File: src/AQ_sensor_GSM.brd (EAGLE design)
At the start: 109.8 x 66.2 mm, 187 parts, among them J1 F-1X03-SIP-100-32, J2 53261-0871, J4 S8411-45R, Q2 MMBT2222, Q3 MMBT2222, Q4 MMBT2222, Q5 MMBT2222, Q6 MMBT2222, Q7 MMBT2222, Q8 FS8205, T1 S8050, T2 S8050, U1 CP2102N-A02-GQFN28, U2 DS1307Z, U3 TP4056, U4 TPS63802DLAR, U5 TXS0108EPWR, U6 TPS63802DLAR, U7 TPS63802DLAR, U8 AMS1117-3.3, X1 ESP32-S3-WROOM-1-N16R8, Y1 32.768kHz

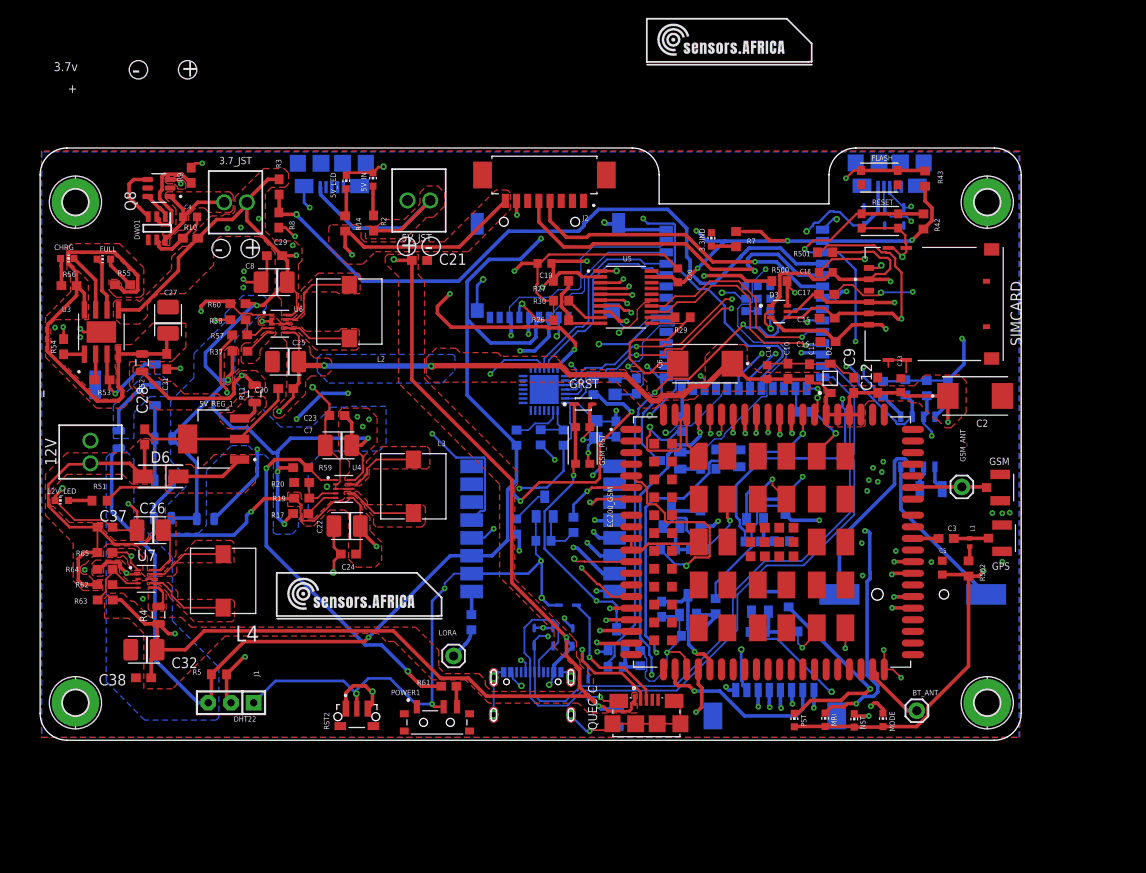
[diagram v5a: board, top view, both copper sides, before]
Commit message: Add 1.8V LDO, EC200UCN Firmware Boot Circuitry, GSM Patch Antenna
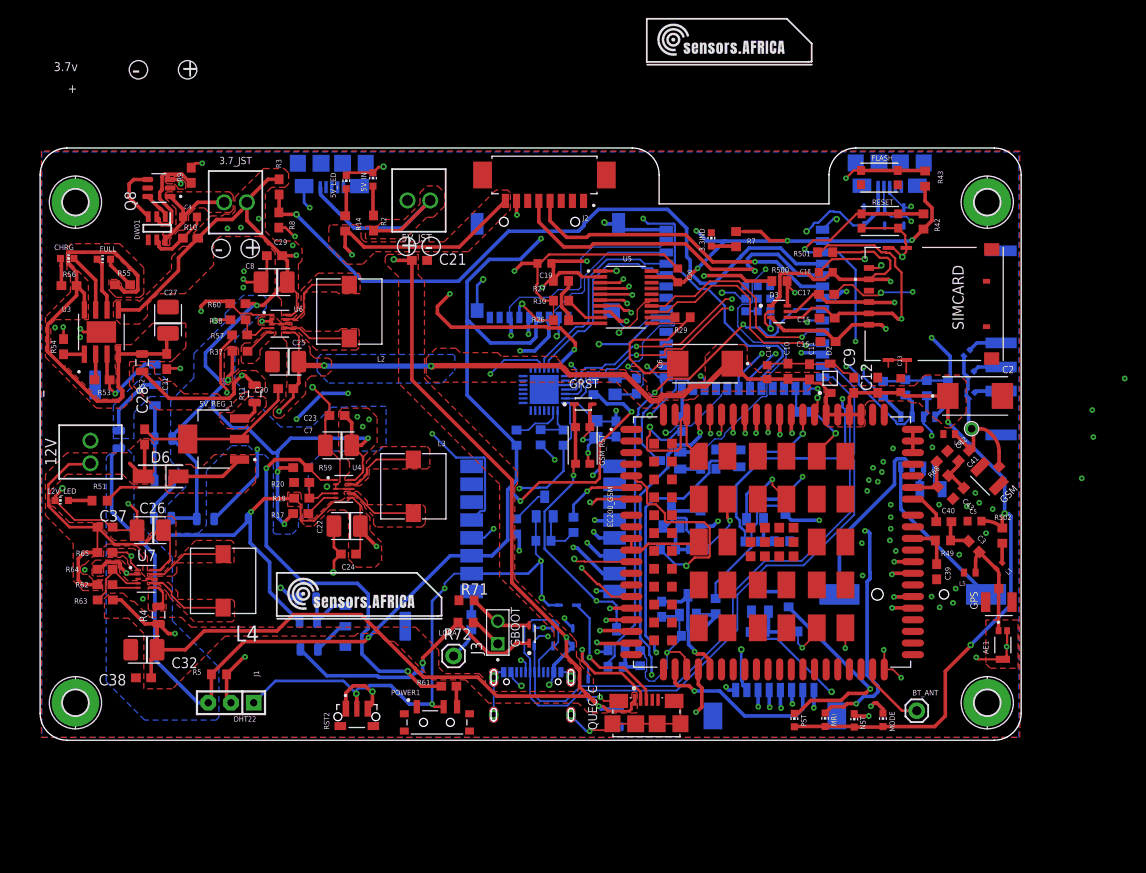
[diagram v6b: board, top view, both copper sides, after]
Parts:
- removed GSM_ANT: 1.9Ghz - 2.4Ghz, SparkFun-Connectors:1X01
- added AE1: W3011, W3011:XDCR_W3011
- added C39, C40, C41, C42, C43: 100pF, SparkFun-Capacitors:0603
- added GBOOT: ON_SEMI_1N4148WSON_SEMI_1N4148WS_0_0, AQ_sensor_GSM:ON_SEMI_1N4148WS_0
- added J3: DS1021-1X2SF162-B, DS1021-1X2SF162-B:CONNFLY_DS1021-1X2SF162-B
- added JUMPVL1.8, R69, R70: 0.4R, Resistor_Capacitor:RES_0805
- added L5, L6: LXES15AAA1-153, LXES15AAA1:INDC1005X45
- added L7, L8, L9: LQW15AN47NG00D, LQW15AN47NG00D 47uh:INDC1005X60N
- added R49, R68: 0R, rcl:R0603
- added R71: 10K, rcl:R0603
- added R72: 1K, rcl:R0603
- added U$107: GSM_SPRING_ANTENNA, GSM_SPRING_ANTENNA:GSM_SPRING_ANTENNA
- added U$109: ADCH002_V1, ADCH002_V1:ADCH002_V1
- added U9: AMS1117-1.8, AMS1117-1.8:SOT229P700X180-4N
- moved GPS 7.17 mm to (108.3, 16.7), turned to 180 degrees
- moved C5 6.33 mm to (105.5, 25.8), turned to 0 degrees
- moved R502 5.27 mm to (108.6, 24.1), turned to 90 degrees
- moved L1 4.20 mm to (108.3, 20.8), turned to 45 degrees
- moved C3 3.23 mm to (105.5, 22.9), turned to 135 degrees
- moved GSM 1.75 mm to (107.2, 30.8), turned to 135 degrees
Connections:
- new net 1.8V: GBOOT.1, R70.1, R72.2
- new net N$156: C3.2, C40.1, R49.1
- new net N$157: C41.2, C43.1, R68.1
- new net N$158: C41.1, GSM.1, L6.1, L7.2, L8.2, L9.2, U$107.1
- new net N$161: L8.1, U$109.3
- new net N$162: L9.1, U$109.2
- new net N$163: L7.1, U$109.4
- new net N$164: JUMPVL1.8.1, R69.1, U9.3
- new net N$165: R70.2, U9.2
- new net N$166: J3.1, R72.1
- net 5V_OUT: now also R69.2
- net GND: now also AE1.2, AE1.3, C39.2, C40.2, C42.2, C43.2, L5.1, L6.2, R71.1, U9.1
- net GNSS_ANT: now also C39.1, R49.2; no longer C3.2
- net GSM_ANT: now also C42.1, R68.2; no longer GSM.1, GSM_ANT.1
- net G_USB_BOOT: now also GBOOT.2, J3.2, R71.2
- net N$10: now also AE1.1, L5.2
- net V_LIPO: now also JUMPVL1.8.2
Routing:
- net G_USB_BOOT: track 19.8 -> 52.7 mm
- net 1.8V: track 0.00 -> 32.2 mm, vias 0 -> 1
- net N$158: track 0.00 -> 20.3 mm
- net GND: track 467.3 -> 479.9 mm, vias 77 -> 95
- net 5V_OUT: track 248.6 -> 260.0 mm
- net N$10: track 3.89 -> 12.1 mm
- net N$164: track 0.00 -> 6.56 mm
- net BOOST_EN: track 95.8 -> 100.7 mm
- net N$157: track 0.00 -> 4.41 mm
- net 12V-IN: track 50.4 -> 46.0 mm
- net N$156: track 0.00 -> 4.17 mm
- net N$165: track 0.00 -> 4.16 mm
- net 4.0V_OUT: track 184.2 -> 188.3 mm, vias 7 -> 8
- net N$162: track 0.00 -> 3.84 mm
- net N$166: track 0.00 -> 3.73 mm
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- added copper zone on layer 1, net X

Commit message: Add Ground clearance for the antenna
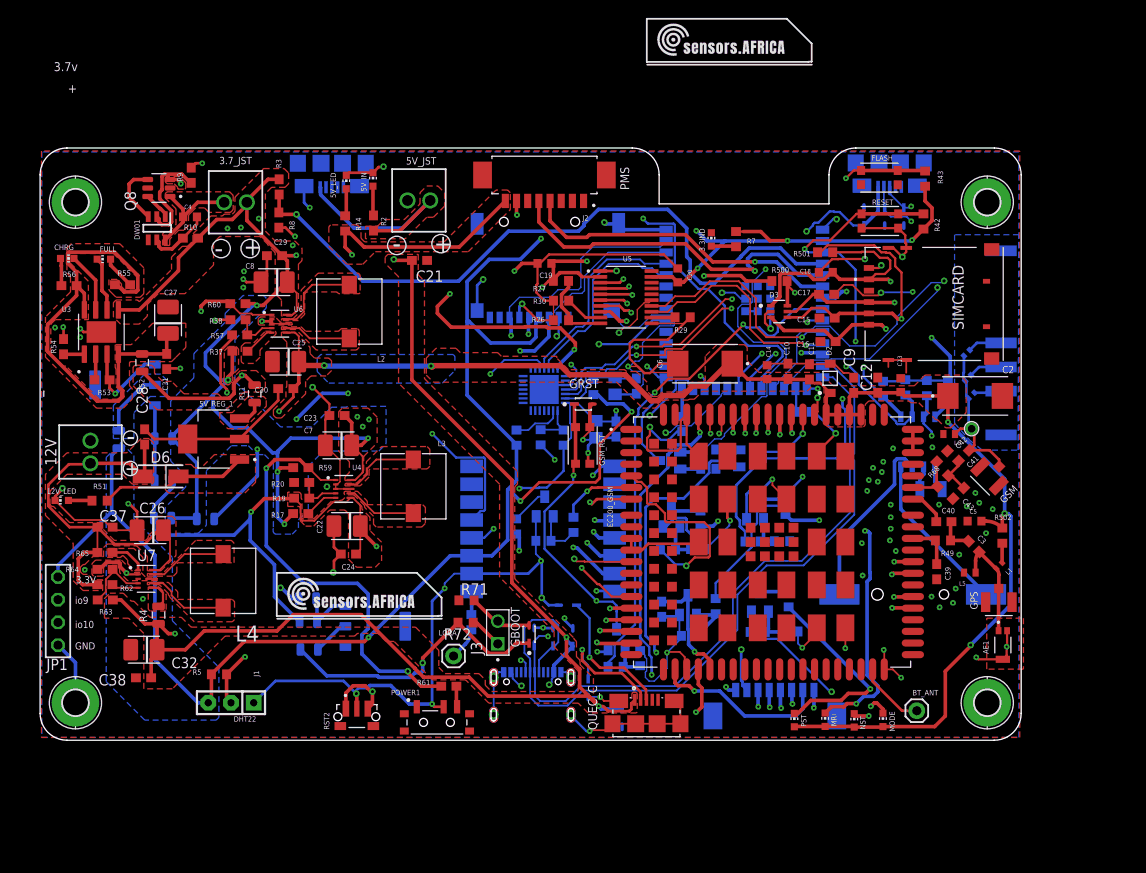
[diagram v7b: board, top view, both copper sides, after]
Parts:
- added JP1: PINHD-1X4, Connector:1X04
- 3.3IND: value (none) -> ORANGE
- BT_ANT: value (none) -> BTANT
- moved L8 0.50 mm to (104.8, 41.8)
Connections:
- new net N$159: R65.1, U7.1
- net +3V3: now also JP1.1
- net BOOST_EN: no longer R65.1, U7.1
- net GND: now also JP1.4
- net IO10: now also JP1.3
- net IO9: now also JP1.2
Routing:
- net IO10: track 0.00 -> 185.6 mm, vias 0 -> 1
- net IO9: track 0.00 -> 179.5 mm, vias 0 -> 1
- net BOOST_EN: track 100.7 -> 82.3 mm, vias 4 -> 3
- net +3V3: track 222.3 -> 232.1 mm
- net 12V-IN: track 46.0 -> 50.4 mm
- net N$159: track 0.00 -> 4.09 mm
- net GND: track 479.9 -> 482.9 mm, vias 95 -> 91
- net N$158: track 20.3 -> 18.7 mm
- net 5V_OUT: track 260.0 -> 259.2 mm
- added copper zone on layer 1, net 34GHB
- added copper zone on layer 16, net KDK
- added copper zone on layer 15, net YT765
- removed copper zone on layer 1, net X
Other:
- board text added: "3.3V"
- board text added: "GND"
- board text added: "PMS"
- board text added: "io10"
- board text added: "io9"
